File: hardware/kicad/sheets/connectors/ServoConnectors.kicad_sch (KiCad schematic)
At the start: 3 parts

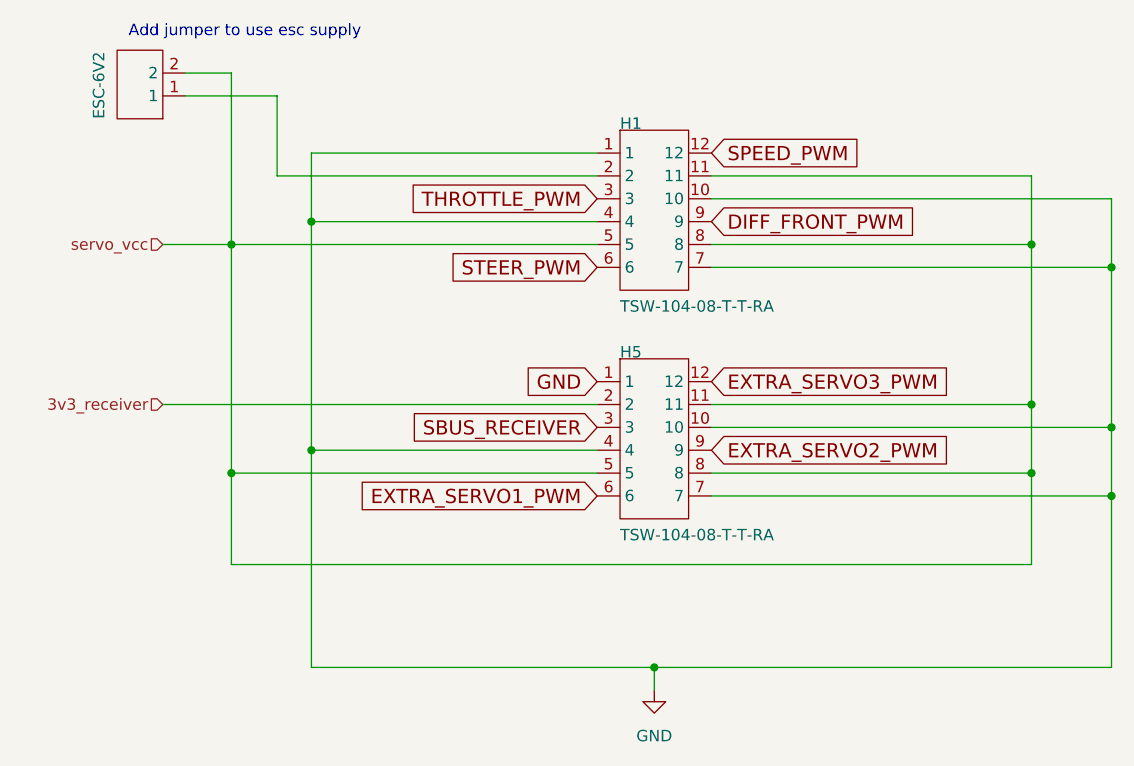
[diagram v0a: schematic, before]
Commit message: organized servo power with better sub sheets
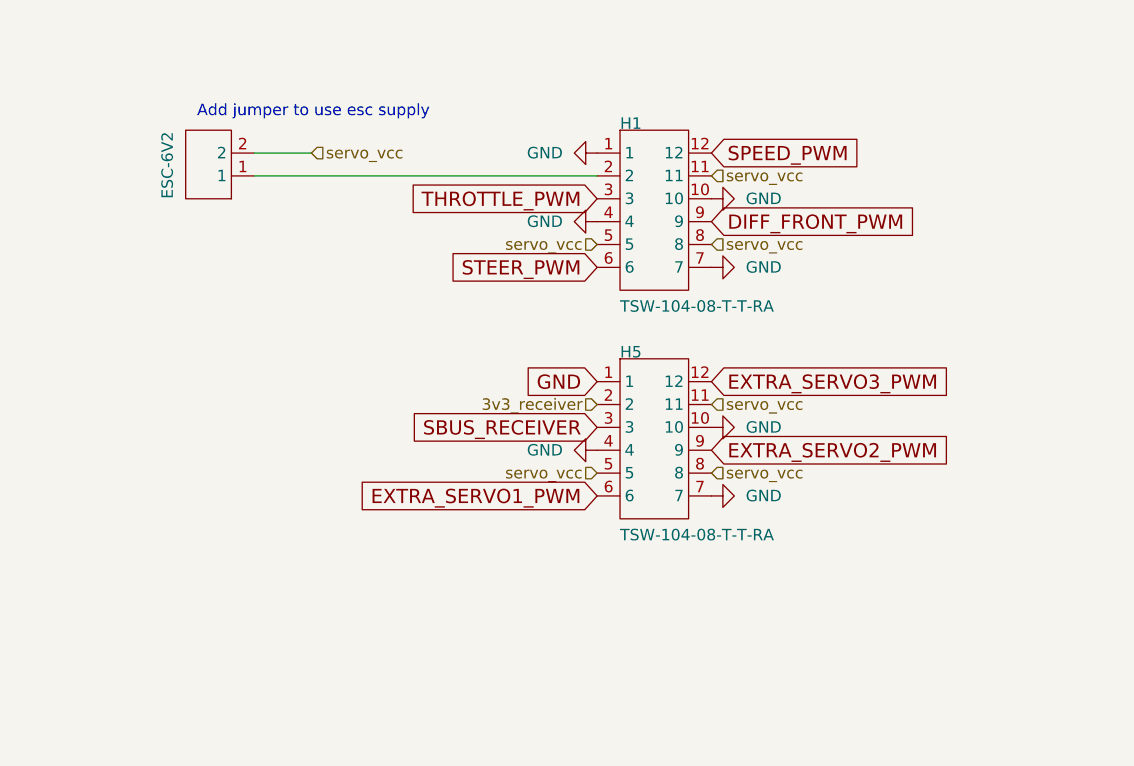
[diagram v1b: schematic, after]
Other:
- moved on the sheet: ESC-6V2

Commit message: resheeted bms and fixed links for the 12v buck
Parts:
- renumbered ESC-6V2 to ESC-6V1, H1 to H5, H5 to H6
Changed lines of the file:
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@@
 		(dnp no)
 		(fields_autoplaced yes)
-		(property "Reference" "#PWR080"
+		(property "Reference" "#PWR086"
 			(at 170.18 91.44 0)
 			(effects
@@
 			(project "svea_powerboard_rev3"
 				(path "/3f85abf4-0b95-4c4a-b7e9-06f59ca1ea3d/5c2e021f-c2d4-49e2-8c36-9a64f1f12005/8d05c3b8-20a4-4a7f-9b20-01f8d5d5be51/5602daa7-78fd-4f1a-8c94-62869666e560"
-					(reference "#PWR080")
+					(reference "#PWR086")
 					(unit 1)
 				)
@@
 		(dnp no)
 		(fields_autoplaced yes)
-		(property "Reference" "#PWR076"
+		(property "Reference" "#PWR083"
 			(at 144.78 86.36 0)
 			(effects
@@
 			(project "svea_powerboard_rev3"
 				(path "/3f85abf4-0b95-4c4a-b7e9-06f59ca1ea3d/5c2e021f-c2d4-49e2-8c36-9a64f1f12005/8d05c3b8-20a4-4a7f-9b20-01f8d5d5be51/5602daa7-78fd-4f1a-8c94-62869666e560"
-					(reference "#PWR076")
+					(reference "#PWR083")
 					(unit 1)
 				)
@@
 		(dnp no)
 		(fields_autoplaced yes)
-		(property "Reference" "#PWR077"
+		(property "Reference" "#PWR084"
 			(at 144.78 111.76 0)
 			(effects
@@
 			(project "svea_powerboard_rev3"
 				(path "/3f85abf4-0b95-4c4a-b7e9-06f59ca1ea3d/5c2e021f-c2d4-49e2-8c36-9a64f1f12005/8d05c3b8-20a4-4a7f-9b20-01f8d5d5be51/5602daa7-78fd-4f1a-8c94-62869666e560"
-					(reference "#PWR077")
+					(reference "#PWR084")
 					(unit 1)
 				)
@@
 		(dnp no)
 		(fields_autoplaced yes)
-		(property "Reference" "#PWR075"
+		(property "Reference" "#PWR082"
 			(at 144.78 78.74 0)
 			(effects
@@
 			(project "svea_powerboard_rev3"
 				(path "/3f85abf4-0b95-4c4a-b7e9-06f59ca1ea3d/5c2e021f-c2d4-49e2-8c36-9a64f1f12005/8d05c3b8-20a4-4a7f-9b20-01f8d5d5be51/5602daa7-78fd-4f1a-8c94-62869666e560"
-					(reference "#PWR075")
+					(reference "#PWR082")
 					(unit 1)
 				)
@@
 		(dnp no)
 		(fields_autoplaced yes)
-		(property "Reference" "#PWR079"
+		(property "Reference" "#PWR087"
 			(at 170.18 109.22 0)
 			(effects
@@
 			(project "svea_powerboard_rev3"
 				(path "/3f85abf4-0b95-4c4a-b7e9-06f59ca1ea3d/5c2e021f-c2d4-49e2-8c36-9a64f1f12005/8d05c3b8-20a4-4a7f-9b20-01f8d5d5be51/5602daa7-78fd-4f1a-8c94-62869666e560"
-					(reference "#PWR079")
+					(reference "#PWR087")
 					(unit 1)
 				)
@@
 		(dnp no)
 		(fields_autoplaced yes)
-		(property "Reference" "#PWR078"
+		(property "Reference" "#PWR088"
 			(at 170.18 116.84 0)
 			(effects
@@
 			(project "svea_powerboard_rev3"
 				(path "/3f85abf4-0b95-4c4a-b7e9-06f59ca1ea3d/5c2e021f-c2d4-49e2-8c36-9a64f1f12005/8d05c3b8-20a4-4a7f-9b20-01f8d5d5be51/5602daa7-78fd-4f1a-8c94-62869666e560"
-					(reference "#PWR078")
+					(reference "#PWR088")
 					(unit 1)
 				)
@@
 		(dnp no)
 		(fields_autoplaced yes)
-		(property "Reference" "#PWR081"
+		(property "Reference" "#PWR085"
 			(at 170.18 83.82 0)
 			(effects
@@
 			(project "svea_powerboard_rev3"
 				(path "/3f85abf4-0b95-4c4a-b7e9-06f59ca1ea3d/5c2e021f-c2d4-49e2-8c36-9a64f1f12005/8d05c3b8-20a4-4a7f-9b20-01f8d5d5be51/5602daa7-78fd-4f1a-8c94-62869666e560"
-					(reference "#PWR081")
+					(reference "#PWR085")
 					(unit 1)
 				)
@@
 		(on_board yes)
 		(dnp no)
-		(property "Reference" "H1"
+		(property "Reference" "H5"
 			(at 153.67 76.2 0)
 			(effects
@@
 			(project "svea_powerboard_rev3"
 				(path "/3f85abf4-0b95-4c4a-b7e9-06f59ca1ea3d/5c2e021f-c2d4-49e2-8c36-9a64f1f12005/8d05c3b8-20a4-4a7f-9b20-01f8d5d5be51/5602daa7-78fd-4f1a-8c94-62869666e560"
-					(reference "H1")
+					(reference "H5")
 					(unit 1)
 				)
@@
 		(on_board yes)
 		(dnp no)
-		(property "Reference" "H5"
+		(property "Reference" "H6"
 			(at 153.67 101.6 0)
 			(effects
@@
 			(project "svea_powerboard_rev3"
 				(path "/3f85abf4-0b95-4c4a-b7e9-06f59ca1ea3d/5c2e021f-c2d4-49e2-8c36-9a64f1f12005/8d05c3b8-20a4-4a7f-9b20-01f8d5d5be51/5602daa7-78fd-4f1a-8c94-62869666e560"
-					(reference "H5")
+					(reference "H6")
 					(unit 1)
 				)
@@
 		(on_board yes)
 		(dnp no)
-		(property "Reference" "ESC-6V2"
+		(property "Reference" "ESC-6V1"
 			(at 104.14 83.82 90)
 			(effects
@@
 			(project "svea_powerboard_rev3"
 				(path "/3f85abf4-0b95-4c4a-b7e9-06f59ca1ea3d/5c2e021f-c2d4-49e2-8c36-9a64f1f12005/8d05c3b8-20a4-4a7f-9b20-01f8d5d5be51/5602daa7-78fd-4f1a-8c94-62869666e560"
-					(reference "ESC-6V2")
-					(unit 1)
-				)
+					(reference "ESC-6V1")
+					(unit 1)
+				)

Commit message: various improvements
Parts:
- renumbered H5 to H2, H6 to H3
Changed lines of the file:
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@@
 		(dnp no)
 		(fields_autoplaced yes)
-		(property "Reference" "#PWR085"
+		(property "Reference" "#PWR0105"
 			(at 170.18 91.44 0)
 			(effects
@@
 			(project "svea_powerboard_rev3"
 				(path "/3f85abf4-0b95-4c4a-b7e9-06f59ca1ea3d/5c2e021f-c2d4-49e2-8c36-9a64f1f12001/e0f45e16-4740-446f-ae55-03461fa88791"
-					(reference "#PWR085")
+					(reference "#PWR0105")
 					(unit 1)
 				)
@@
 		(dnp no)
 		(fields_autoplaced yes)
-		(property "Reference" "#PWR082"
+		(property "Reference" "#PWR0102"
 			(at 144.78 86.36 0)
 			(effects
@@
 			(project "svea_powerboard_rev3"
 				(path "/3f85abf4-0b95-4c4a-b7e9-06f59ca1ea3d/5c2e021f-c2d4-49e2-8c36-9a64f1f12001/e0f45e16-4740-446f-ae55-03461fa88791"
-					(reference "#PWR082")
+					(reference "#PWR0102")
 					(unit 1)
 				)
@@
 		(dnp no)
 		(fields_autoplaced yes)
-		(property "Reference" "#PWR083"
+		(property "Reference" "#PWR0103"
 			(at 144.78 111.76 0)
 			(effects
@@
 			(project "svea_powerboard_rev3"
 				(path "/3f85abf4-0b95-4c4a-b7e9-06f59ca1ea3d/5c2e021f-c2d4-49e2-8c36-9a64f1f12001/e0f45e16-4740-446f-ae55-03461fa88791"
-					(reference "#PWR083")
+					(reference "#PWR0103")
 					(unit 1)
 				)
@@
 		(dnp no)
 		(fields_autoplaced yes)
-		(property "Reference" "#PWR071"
+		(property "Reference" "#PWR0101"
 			(at 144.78 78.74 0)
 			(effects
@@
 			(project "svea_powerboard_rev3"
 				(path "/3f85abf4-0b95-4c4a-b7e9-06f59ca1ea3d/5c2e021f-c2d4-49e2-8c36-9a64f1f12001/e0f45e16-4740-446f-ae55-03461fa88791"
-					(reference "#PWR071")
+					(reference "#PWR0101")
 					(unit 1)
 				)
@@
 		(dnp no)
 		(fields_autoplaced yes)
-		(property "Reference" "#PWR086"
+		(property "Reference" "#PWR0106"
 			(at 170.18 109.22 0)
 			(effects
@@
 			(project "svea_powerboard_rev3"
 				(path "/3f85abf4-0b95-4c4a-b7e9-06f59ca1ea3d/5c2e021f-c2d4-49e2-8c36-9a64f1f12001/e0f45e16-4740-446f-ae55-03461fa88791"
-					(reference "#PWR086")
+					(reference "#PWR0106")
 					(unit 1)
 				)
@@
 		(dnp no)
 		(fields_autoplaced yes)
-		(property "Reference" "#PWR087"
+		(property "Reference" "#PWR0107"
 			(at 170.18 116.84 0)
 			(effects
@@
 			(project "svea_powerboard_rev3"
 				(path "/3f85abf4-0b95-4c4a-b7e9-06f59ca1ea3d/5c2e021f-c2d4-49e2-8c36-9a64f1f12001/e0f45e16-4740-446f-ae55-03461fa88791"
-					(reference "#PWR087")
+					(reference "#PWR0107")
 					(unit 1)
 				)
@@
 		(dnp no)
 		(fields_autoplaced yes)
-		(property "Reference" "#PWR084"
+		(property "Reference" "#PWR0104"
 			(at 170.18 83.82 0)
 			(effects
@@
 			(project "svea_powerboard_rev3"
 				(path "/3f85abf4-0b95-4c4a-b7e9-06f59ca1ea3d/5c2e021f-c2d4-49e2-8c36-9a64f1f12001/e0f45e16-4740-446f-ae55-03461fa88791"
-					(reference "#PWR084")
+					(reference "#PWR0104")
 					(unit 1)
 				)
@@
 		(on_board yes)
 		(dnp no)
-		(property "Reference" "H5"
+		(property "Reference" "H2"
 			(at 153.67 76.2 0)
 			(effects
@@
 			(project "svea_powerboard_rev3"
 				(path "/3f85abf4-0b95-4c4a-b7e9-06f59ca1ea3d/5c2e021f-c2d4-49e2-8c36-9a64f1f12001/e0f45e16-4740-446f-ae55-03461fa88791"
-					(reference "H5")
+					(reference "H2")
 					(unit 1)
 				)
@@
 		(on_board yes)
 		(dnp no)
-		(property "Reference" "H6"
+		(property "Reference" "H3"
 			(at 153.67 101.6 0)
 			(effects
@@
 			(project "svea_powerboard_rev3"
 				(path "/3f85abf4-0b95-4c4a-b7e9-06f59ca1ea3d/5c2e021f-c2d4-49e2-8c36-9a64f1f12001/e0f45e16-4740-446f-ae55-03461fa88791"
-					(reference "H6")
-					(unit 1)
-				)
+					(reference "H3")
+					(unit 1)
+				)

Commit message: various improvements
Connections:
- net EXTRA_SERVO3_PWM is gone; now on net 3v3_receiver: H3.12
- net 3v3_receiver: no longer H3.2
- net servo_vcc: now also H3.2; no longer H3.11
- net DIFF_FRONT_PWM renamed SERVO2
- net EXTRA_SERVO1_PWM renamed SERVO5
- net EXTRA_SERVO2_PWM renamed SERVO6
- net SBUS_RECEIVER renamed SERVO4
- net SPEED_PWM renamed SERVO3
- net STEER_PWM renamed SERVO1
- net THROTTLE_PWM renamed THROTTLE_DATA_(SERVO_0)
- new net 3v3_DATA: H3.11

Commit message: current sensing on the servos and cleaning up empty sheets
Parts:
- renumbered H2 to H3, H3 to H4
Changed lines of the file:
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@@
+		(dnp no)
+		(fields_autoplaced yes)
+		(property "Reference" "#PWR0115"
+			(at 170.18 91.44 0)
+			(effects
+				(font
+					(size 1.27 1.27)
+				)
+				(hide yes)
+			)
+		)
+		(property "Value" "GND"
+			(at 167.64 91.4399 90)
+			(effects
+				(font
+					(size 1.27 1.27)
+				)
+				(justify right)
+			)
+		)
+		(property "Footprint" ""
+			(at 163.83 91.44 0)
+			(effects
+				(font
+					(size 1.27 1.27)
+				)
+				(hide yes)
+			)
+		)
+		(property "Datasheet" ""
+			(at 163.83 91.44 0)
+			(effects
+				(font
+					(size 1.27 1.27)
+				)
+				(hide yes)
+			)
+		)
+		(property "Description" "Power symbol creates a global label with name \"GND\" , ground"
+			(at 163.83 91.44 0)
+			(effects
+				(font
+					(size 1.27 1.27)
+				)
+				(hide yes)
+			)
+		)
+		(pin "1"
+		)
+		(instances
+			(project "svea_powerboard_rev3"
+				(path "/3f85abf4-0b95-4c4a-b7e9-06f59ca1ea3d/5c2e021f-c2d4-49e2-8c36-9a64f1f12001/e0f45e16-4740-446f-ae55-03461fa88791"
+					(reference "#PWR0115")
+					(unit 1)
+				)
+			)
+		)
+	)
+	(symbol
+		(lib_id "power:GND")
+		(at 151.13 86.36 270)
+		(unit 1)
+		(exclude_from_sim no)
+		(in_bom yes)
+		(on_board yes)
+		(dnp no)
+		(fields_autoplaced yes)
+		(property "Reference" "#PWR0111"
+			(at 144.78 86.36 0)
+			(effects
+				(font
+					(size 1.27 1.27)
+				)
+				(hide yes)
+			)
+		)
+		(property "Value" "GND"
+			(at 147.32 86.3599 90)
+			(effects
+				(font
+					(size 1.27 1.27)
+				)
+				(justify right)
+			)
+		)
+		(property "Footprint" ""
+			(at 151.13 86.36 0)
+			(effects
+				(font
+					(size 1.27 1.27)
+				)
+				(hide yes)
+			)
+		)
+		(property "Datasheet" ""
+			(at 151.13 86.36 0)
+			(effects
+				(font
+					(size 1.27 1.27)
+				)
+				(hide yes)
+			)
+		)
+		(property "Description" "Power symbol creates a global label with name \"GND\" , ground"
+			(at 151.13 86.36 0)
+			(effects
+				(font
+					(size 1.27 1.27)
+				)
+				(hide yes)
+			)
+		)
+		(pin "1"
+		)
+		(instances
+			(project "svea_powerboard_rev3"
+				(path "/3f85abf4-0b95-4c4a-b7e9-06f59ca1ea3d/5c2e021f-c2d4-49e2-8c36-9a64f1f12001/e0f45e16-4740-446f-ae55-03461fa88791"
+					(reference "#PWR0111")
+					(unit 1)
+				)
+			)
+		)
+	)
+	(symbol
+		(lib_id "power:GND")
+		(at 151.13 111.76 270)
+		(unit 1)
+		(exclude_from_sim no)
+		(in_bom yes)
+		(on_board yes)
 		(dnp no)
 		(fields_autoplaced yes)
 		(property "Reference" "#PWR0113"
-			(at 170.18 91.44 0)
+			(at 144.78 111.76 0)
 			(effects
 				(font
@@
 		)
 		(property "Value" "GND"
-			(at 167.64 91.4399 90)
+			(at 147.32 111.7599 90)
 			(effects
 				(font
@@
 		)
 		(property "Footprint" ""
-			(at 163.83 91.44 0)
+			(at 151.13 111.76 0)
 			(effects
 				(font
@@
 		)
 		(property "Datasheet" ""
-			(at 163.83 91.44 0)
+			(at 151.13 111.76 0)
 			(effects
 				(font
@@
 		)
 		(property "Description" "Power symbol creates a global label with name \"GND\" , ground"
-			(at 163.83 91.44 0)
+			(at 151.13 111.76 0)
 			(effects
 				(font
@@
 	(symbol
 		(lib_id "power:GND")
-		(at 151.13 86.36 270)
+		(at 151.13 78.74 270)
 		(unit 1)
 		(exclude_from_sim no)
@@
 		(fields_autoplaced yes)
 		(property "Reference" "#PWR0110"
-			(at 144.78 86.36 0)
-			(effects
-				(font
-					(size 1.27 1.27)
-				)
-				(hide yes)
-			)
-		)
-		(property "Value" "GND"
-			(at 147.32 86.3599 90)
-			(effects
-				(font
-					(size 1.27 1.27)
-				)
-				(justify right)
-			)
-		)
-		(property "Footprint" ""
-			(at 151.13 86.36 0)
-			(effects
-				(font
-					(size 1.27 1.27)
-				)
-				(hide yes)
-			)
-		)
-		(property "Datasheet" ""
-			(at 151.13 86.36 0)
-			(effects
-				(font
-					(size 1.27 1.27)
-				)
-				(hide yes)
-			)
-		)
-		(property "Description" "Power symbol creates a global label with name \"GND\" , ground"
-			(at 151.13 86.36 0)
-			(effects
-				(font
-					(size 1.27 1.27)
-				)
-				(hide yes)
-			)
-		)
-		(pin "1"
-		)
-		(instances
-			(project "svea_powerboard_rev3"
-				(path "/3f85abf4-0b95-4c4a-b7e9-06f59ca1ea3d/5c2e021f-c2d4-49e2-8c36-9a64f1f12001/e0f45e16-4740-446f-ae55-03461fa88791"
-					(reference "#PWR0110")
-					(unit 1)
-				)
-			)
-		)
-	)
-	(symbol
-		(lib_id "power:GND")
-		(at 151.13 111.76 270)
-		(unit 1)
-		(exclude_from_sim no)
-		(in_bom yes)
-		(on_board yes)
-		(dnp no)
-		(fields_autoplaced yes)
-		(property "Reference" "#PWR0111"
-			(at 144.78 111.76 0)
-			(effects
-				(font
-					(size 1.27 1.27)
-				)
-				(hide yes)
-			)
-		)
-		(property "Value" "GND"
-			(at 147.32 111.7599 90)
-			(effects
-				(font
-					(size 1.27 1.27)
-				)
-				(justify right)
-			)
-		)
-		(property "Footprint" ""
-			(at 151.13 111.76 0)
-			(effects
-				(font
-					(size 1.27 1.27)
-				)
-				(hide yes)
-			)
-		)
-		(property "Datasheet" ""
-			(at 151.13 111.76 0)
-			(effects
-				(font
-					(size 1.27 1.27)
-				)
-				(hide yes)
-			)
-		)
-		(property "Description" "Power symbol creates a global label with name \"GND\" , ground"
-			(at 151.13 111.76 0)
-			(effects
-				(font
-					(size 1.27 1.27)
-				)
-				(hide yes)
-			)
-		)
-		(pin "1"
-		)
-		(instances
-			(project "svea_powerboard_rev3"
-				(path "/3f85abf4-0b95-4c4a-b7e9-06f59ca1ea3d/5c2e021f-c2d4-49e2-8c36-9a64f1f12001/e0f45e16-4740-446f-ae55-03461fa88791"
-					(reference "#PWR0111")
-					(unit 1)
-				)
-			)
-		)
-	)
-	(symbol
-		(lib_id "power:GND")
-		(at 151.13 78.74 270)
-		(unit 1)
-		(exclude_from_sim no)
-		(in_bom yes)
-		(on_board yes)
-		(dnp no)
-		(fields_autoplaced yes)
-		(property "Reference" "#PWR0109"
 			(at 144.78 78.74 0)
 			(effects
@@
 			(project "svea_powerboard_rev3"
 				(path "/3f85abf4-0b95-4c4a-b7e9-06f59ca1ea3d/5c2e021f-c2d4-49e2-8c36-9a64f1f12001/e0f45e16-4740-446f-ae55-03461fa88791"
-					(reference "#PWR0109")
+					(reference "#PWR0110")
 					(unit 1)
 				)
@@
 		(dnp no)
 		(fields_autoplaced yes)
-		(property "Reference" "#PWR0114"
+		(property "Reference" "#PWR0116"
 			(at 170.18 109.22 0)
 			(effects
@@
 			(project "svea_powerboard_rev3"
 				(path "/3f85abf4-0b95-4c4a-b7e9-06f59ca1ea3d/5c2e021f-c2d4-49e2-8c36-9a64f1f12001/e0f45e16-4740-446f-ae55-03461fa88791"
-					(reference "#PWR0114")
+					(reference "#PWR0116")
 					(unit 1)
 				)
@@
 		(dnp no)
 		(fields_autoplaced yes)
-		(property "Reference" "#PWR0115"
+		(property "Reference" "#PWR0117"
 			(at 170.18 116.84 0)
 			(effects
@@
 			(project "svea_powerboard_rev3"
 				(path "/3f85abf4-0b95-4c4a-b7e9-06f59ca1ea3d/5c2e021f-c2d4-49e2-8c36-9a64f1f12001/e0f45e16-4740-446f-ae55-03461fa88791"
-					(reference "#PWR0115")
+					(reference "#PWR0117")
 					(unit 1)
 				)
@@
 		(dnp no)
 		(fields_autoplaced yes)
-		(property "Reference" "#PWR0178"
+		(property "Reference" "#PWR0112"
 			(at 144.78 104.14 0)
 			(effects
@@
 			(project "svea_powerboard_rev3"
 				(path "/3f85abf4-0b95-4c4a-b7e9-06f59ca1ea3d/5c2e021f-c2d4-49e2-8c36-9a64f1f12001/e0f45e16-4740-446f-ae55-03461fa88791"
-					(reference "#PWR0178")
+					(reference "#PWR0112")
 					(unit 1)
 				)
@@
 		(dnp no)
 		(fields_autoplaced yes)
-		(property "Reference" "#PWR0112"
+		(property "Reference" "#PWR0114"
 			(at 170.18 83.82 0)
 			(effects
@@
 			(project "svea_powerboard_rev3"
 				(path "/3f85abf4-0b95-4c4a-b7e9-06f59ca1ea3d/5c2e021f-c2d4-49e2-8c36-9a64f1f12001/e0f45e16-4740-446f-ae55-03461fa88791"
-					(reference "#PWR0112")
+					(reference "#PWR0114")
 					(unit 1)
 				)
@@
 		(on_board yes)
 		(dnp no)
-		(property "Reference" "H2"
+		(property "Reference" "H3"
 			(at 153.67 76.2 0)
 			(effects
@@
 			(project "svea_powerboard_rev3"
 				(path "/3f85abf4-0b95-4c4a-b7e9-06f59ca1ea3d/5c2e021f-c2d4-49e2-8c36-9a64f1f12001/e0f45e16-4740-446f-ae55-03461fa88791"
-					(reference "H2")
+					(reference "H3")
 					(unit 1)
 				)
@@
 		(on_board yes)
 		(dnp no)
-		(property "Reference" "H3"
+		(property "Reference" "H4"
 			(at 153.67 101.6 0)
 			(effects
@@
 			(project "svea_powerboard_rev3"
 				(path "/3f85abf4-0b95-4c4a-b7e9-06f59ca1ea3d/5c2e021f-c2d4-49e2-8c36-9a64f1f12001/e0f45e16-4740-446f-ae55-03461fa88791"
-					(reference "H3")
-					(unit 1)
-				)
+					(reference "H4")
+					(unit 1)
+				)

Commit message: pre robot updating references
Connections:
- net 3v3_receiver renamed 3v3
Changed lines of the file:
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@@
+		)
+	)
+	(wire
+		(pts
+			(xy 181.61 109.22) (xy 181.61 111.76)
+		)
+		(stroke
+			(width 0)
+			(type default)
+		)
+	)
+	(wire
+		(pts
+			(xy 163.83 109.22) (xy 181.61 109.22)
+		)
+		(stroke
+			(width 0)
+			(type default)
 		)
 	)
@@
 		)
 	)
-	(hierarchical_label "GND"
-		(shape input)
-		(at 163.83 109.22 0)
-		(effects
-			(font
-				(size 1.27 1.27)
-			)
-			(justify left)
-		)
-	)
-	(hierarchical_label "3v3_receiver"
+	(hierarchical_label "3v3"
 		(shape input)
 		(at 163.83 104.14 0)
@@
 		)
 	)
+	(symbol
+		(lib_id "power:GND")
+		(at 181.61 111.76 0)
+		(unit 1)
+		(exclude_from_sim no)
+		(in_bom yes)
+		(on_board yes)
+		(dnp no)
+		(fields_autoplaced yes)
+		(property "Reference" "#PWR0120"
+			(at 181.61 118.11 0)
+			(effects
+				(font
+					(size 1.27 1.27)
+				)
+				(hide yes)
+			)
+		)
+		(property "Value" "GND"
+			(at 181.61 116.84 0)
+			(effects
+				(font
+					(size 1.27 1.27)
+				)
+			)
+		)
+		(property "Footprint" ""
+			(at 181.61 111.76 0)
+			(effects
+				(font
+					(size 1.27 1.27)
+				)
+				(hide yes)
+			)
+		)
+		(property "Datasheet" ""
+			(at 181.61 111.76 0)
+			(effects
+				(font
+					(size 1.27 1.27)
+				)
+				(hide yes)
+			)
+		)
+		(property "Description" "Power symbol creates a global label with name \"GND\" , ground"
+			(at 181.61 111.76 0)
+			(effects
+				(font
+					(size 1.27 1.27)
+				)
+				(hide yes)
+			)
+		)
+		(pin "1"
+		)
+		(instances
+			(project ""
+				(path "/3f85abf4-0b95-4c4a-b7e9-06f59ca1ea3d/5c2e021f-c2d4-49e2-8c36-9a64f1f12001/e0f45e16-4740-446f-ae55-03461fa88791"
+					(reference "#PWR0120")
+					(unit 1)
+				)
+			)
+		)
+	)
